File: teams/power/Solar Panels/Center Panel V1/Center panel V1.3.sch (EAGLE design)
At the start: 9 parts

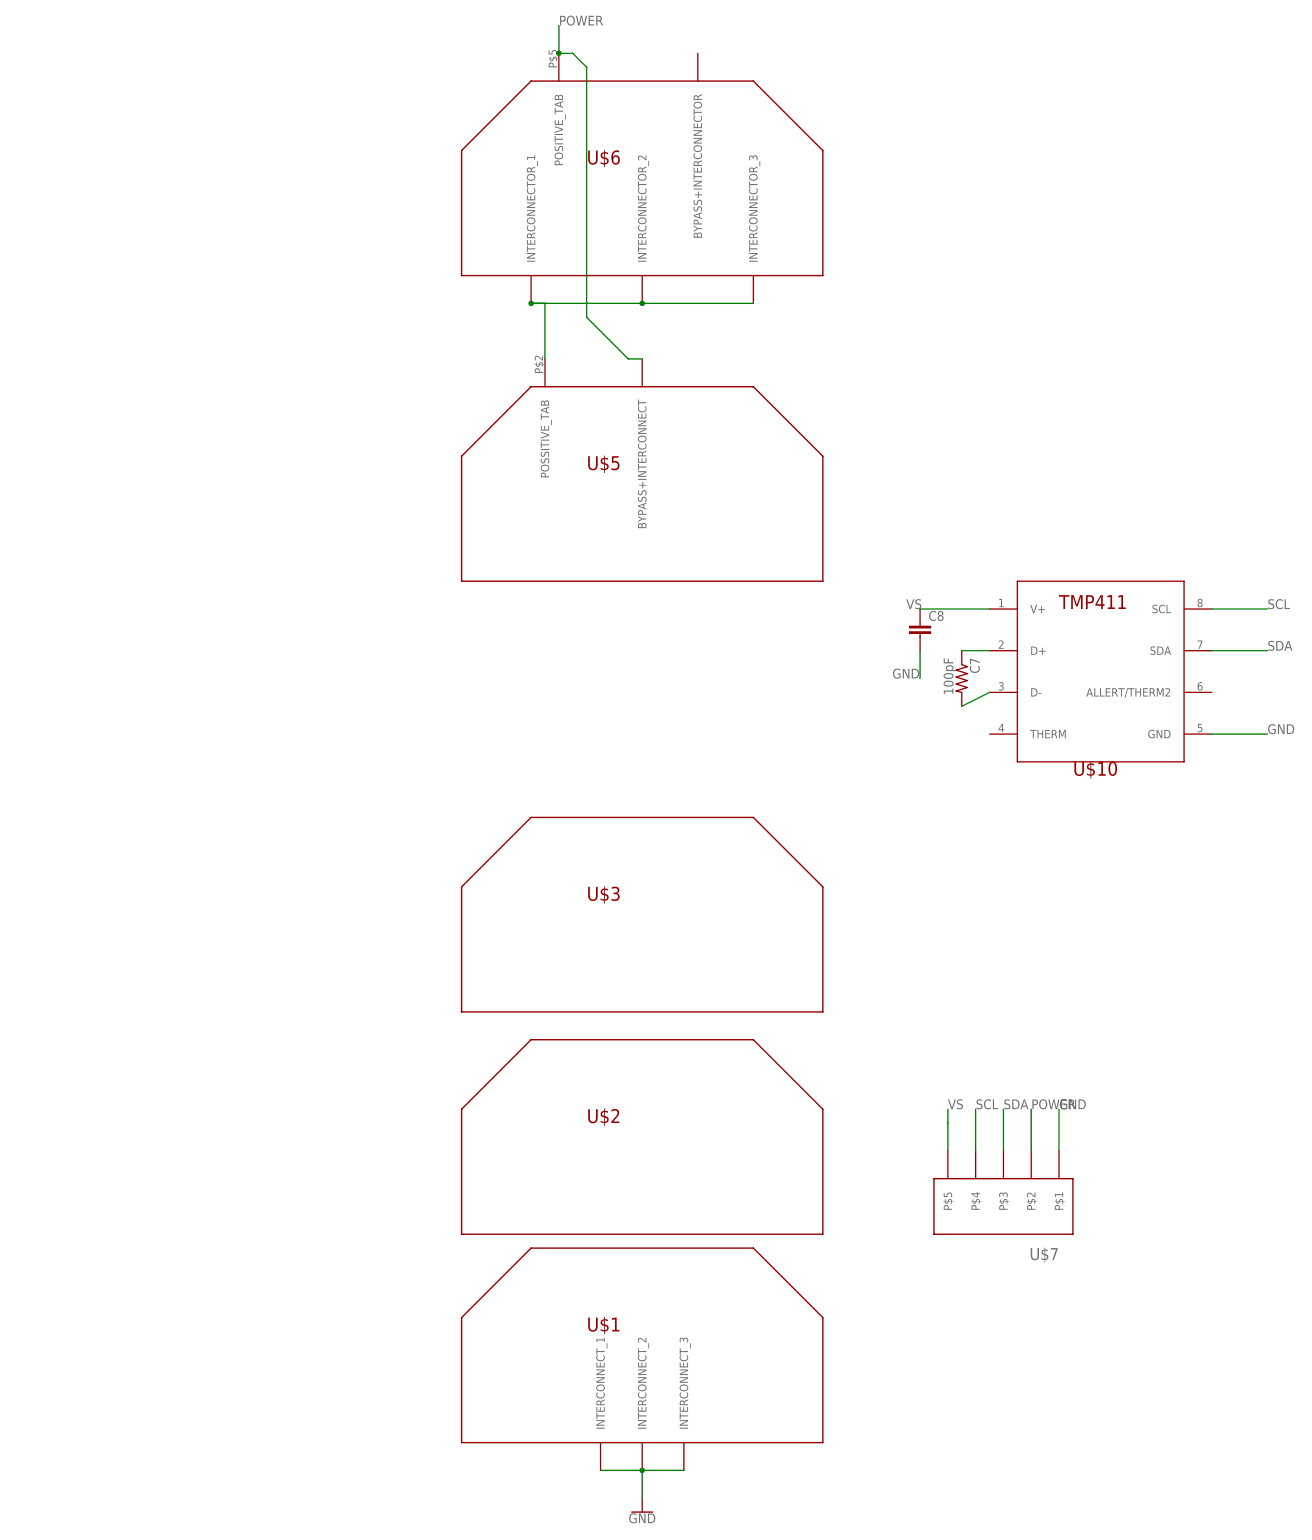
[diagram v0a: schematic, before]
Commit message: EPS/ old panels: Remove ground plane and changed temp sensor to TMP36
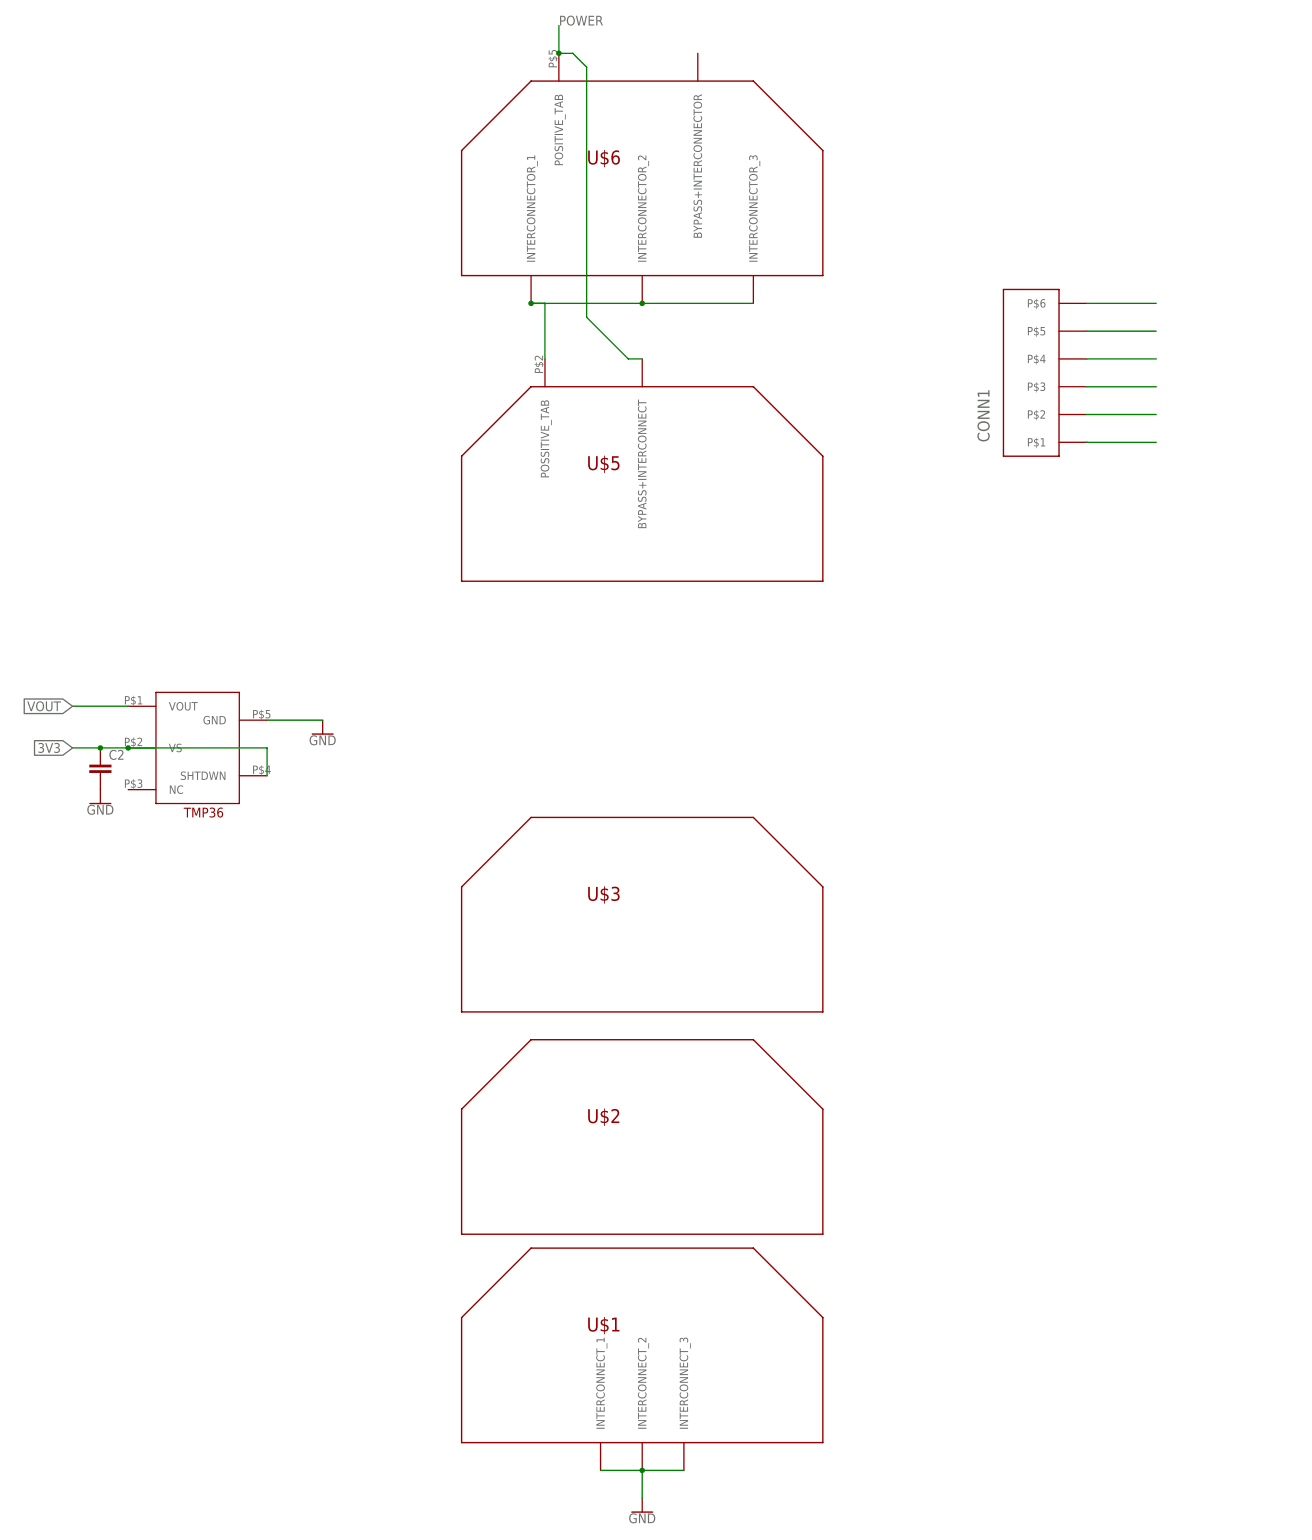
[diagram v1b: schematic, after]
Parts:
- removed C7: 100pF, Battery board V4.1 - simple signals:R-US_R0805
- removed C8: (no value), Battery board V4.1 - simple signals:C
- removed U$10: TMP411, DubSat1 Components:TMP411
- added C2: (no value), DubSat1 Components:CAPACITOR0805
- added CONN1: PICOLOCK_6, DubSat1 Components:PICOLOCK_6
- U$7: value PICOLOCK_5 -> TMP36; device DubSat1 Components:PICOLOCK_5 -> DubSat1 Components:TMP36
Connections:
- removed net N$14: C7.1, U$10.D+
- removed net N$15: C7.2, U$10.D-
- removed net SCL: U$10.SCL, U$7.P$4
- removed net SDA: U$10.SDA, U$7.P$3
- removed net VS: C8.1, U$10.V+, U$7.P$5
- new net 3V3: C2.1, CONN1.P$3, U$7.SHTDWN, U$7.VS
- new net VOUT: CONN1.P$4, U$7.VOUT
- net GND: now also CONN1.P$2, CONN1.P$5, U$7.GND; no longer C8.2, U$10.GND, U$7.P$1
- net POWER: now also CONN1.P$1, CONN1.P$6; no longer U$7.P$2
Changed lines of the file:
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@@
 <?xml version="1.0" encoding="utf-8"?>
 <!DOCTYPE eagle SYSTEM "eagle.dtd">
-<eagle version="8.3.1">
+<eagle version="8.5.0">
 <drawing>
 <settings>
@@
 <layer number="59" name="tCarbon" color="7" fill="1" visible="no" active="no"/>
 <layer number="60" name="bCarbon" color="7" fill="1" visible="no" active="no"/>
+<layer number="88" name="SimResults" color="9" fill="1" visible="yes" active="yes"/>
+<layer number="89" name="SimProbes" color="9" fill="1" visible="yes" active="yes"/>
 <layer number="90" name="Modules" color="5" fill="1" visible="yes" active="yes"/>
 <layer number="91" name="Nets" color="2" fill="1" visible="yes" active="yes"/>
@@
 <part name="U$6" library="DubSat1 Components" library_urn="urn:adsk.eagle:library:348159" deviceset="SOLAR_CELL_STAND-ALONE" device="" package3d_urn="urn:adsk.eagle:package:348283/2"/>
 <part name="GND1" library="SparkFun-PowerSymbols" deviceset="GND" device=""/>
-<part name="U$7" library="DubSat1 Components" library_urn="urn:adsk.eagle:library:348159" deviceset="PICOLOCK_5" device="" package3d_urn="urn:adsk.eagle:package:348289/2"/>
-<part name="U$10" library="DubSat1 Components" deviceset="TMP411" device=""/>
-<part name="C7" library="Battery board V4.1 - simple signals" deviceset="R-US_" device="R0805" value="100pF"/>
-<part name="C8" library="Battery board V4.1 - simple signals" deviceset="C" device=""/>
+<part name="U$7" library="DubSat1 Components" deviceset="TMP36" device=""/>
+<part name="C2" library="DubSat1 Components" deviceset="CAPACITOR" device="0805"/>
+<part name="GND4" library="SparkFun-PowerSymbols" deviceset="GND" device=""/>
+<part name="GND5" library="SparkFun-PowerSymbols" deviceset="GND" device=""/>
+<part name="CONN1" library="DubSat1 Components" deviceset="PICOLOCK_6" device=""/>
 </parts>
 <sheets>
@@
 <instance part="U$6" gate="G$1" x="0" y="213.36"/>
 <instance part="GND1" gate="1" x="33.02" y="-12.7"/>
-<instance part="U$7" gate="G$1" x="96.52" y="48.26" rot="R180"/>
-<instance part="U$10" gate="G$1" x="116.84" y="139.7"/>
-<instance part="C7" gate="G$1" x="91.44" y="139.7" rot="R270"/>
-<instance part="C8" gate="G$1" x="83.82" y="149.86"/>
+<instance part="U$7" gate="G$1" x="-48.26" y="127"/>
+<instance part="C2" gate="G$1" x="-66.04" y="121.92"/>
+<instance part="GND4" gate="1" x="-66.04" y="116.84"/>
+<instance part="GND5" gate="1" x="-25.4" y="129.54"/>
+<instance part="CONN1" gate="G$1" x="109.22" y="195.58" rot="R90"/>
 </instances>
 <busses>
@@
 </segment>
 <segment>
-<pinref part="U$7" gate="G$1" pin="P$1"/>
-<wire x1="109.22" y1="53.34" x2="109.22" y2="60.96" width="0.1524" layer="91"/>
-<label x="109.22" y="60.96" size="1.778" layer="95"/>
-</segment>
-<segment>
-<pinref part="U$10" gate="G$1" pin="GND"/>
-<wire x1="137.16" y1="129.54" x2="147.32" y2="129.54" width="0.1524" layer="91"/>
-<label x="147.32" y="129.54" size="1.778" layer="95"/>
-</segment>
-<segment>
-<pinref part="C8" gate="G$1" pin="2"/>
-<wire x1="83.82" y1="144.78" x2="83.82" y2="139.7" width="0.1524" layer="91"/>
-<label x="78.74" y="139.7" size="1.778" layer="95"/>
+<pinref part="U$7" gate="G$1" pin="GND"/>
+<wire x1="-35.56" y1="132.08" x2="-25.4" y2="132.08" width="0.1524" layer="91"/>
+<pinref part="GND5" gate="1" pin="GND"/>
+</segment>
+<segment>
+<pinref part="CONN1" gate="G$1" pin="P$5"/>
+<wire x1="114.3" y1="203.2" x2="127" y2="203.2" width="0.1524" layer="91"/>
+</segment>
+<segment>
+<pinref part="CONN1" gate="G$1" pin="P$2"/>
+<wire x1="114.3" y1="187.96" x2="127" y2="187.96" width="0.1524" layer="91"/>
 </segment>
 </net>
@@
 </segment>
 </net>
-<net name="VS" class="0">
-<segment>
-<pinref part="U$7" gate="G$1" pin="P$5"/>
-<wire x1="88.9" y1="53.34" x2="88.9" y2="58.42" width="0.1524" layer="91"/>
-<wire x1="88.9" y1="60.96" x2="88.9" y2="58.42" width="0.1524" layer="91"/>
-<label x="88.9" y="60.96" size="1.778" layer="95"/>
-</segment>
-<segment>
-<pinref part="U$10" gate="G$1" pin="V+"/>
-<wire x1="96.52" y1="152.4" x2="83.82" y2="152.4" width="0.1524" layer="91"/>
-<label x="81.28" y="152.4" size="1.778" layer="95"/>
-<pinref part="C8" gate="G$1" pin="1"/>
-</segment>
-</net>
-<net name="SDA" class="0">
-<segment>
-<pinref part="U$7" gate="G$1" pin="P$3"/>
-<wire x1="99.06" y1="53.34" x2="99.06" y2="60.96" width="0.1524" layer="91"/>
-<label x="99.06" y="60.96" size="1.778" layer="95"/>
-</segment>
-<segment>
-<pinref part="U$10" gate="G$1" pin="SDA"/>
-<wire x1="137.16" y1="144.78" x2="147.32" y2="144.78" width="0.1524" layer="91"/>
-<label x="147.32" y="144.78" size="1.778" layer="95"/>
-</segment>
-</net>
-<net name="SCL" class="0">
-<segment>
-<pinref part="U$7" gate="G$1" pin="P$4"/>
-<wire x1="93.98" y1="53.34" x2="93.98" y2="60.96" width="0.1524" layer="91"/>
-<label x="93.98" y="60.96" size="1.778" layer="95"/>
-</segment>
-<segment>
-<pinref part="U$10" gate="G$1" pin="SCL"/>
-<wire x1="137.16" y1="152.4" x2="147.32" y2="152.4" width="0.1524" layer="91"/>
-<label x="147.32" y="152.4" size="1.778" layer="95"/>
-</segment>
-</net>
 <net name="POWER" class="0">
-<segment>
-<pinref part="U$7" gate="G$1" pin="P$2"/>
-<wire x1="104.14" y1="53.34" x2="104.14" y2="60.96" width="0.1524" layer="91"/>
-<label x="104.14" y="60.96" size="1.778" layer="95"/>
-</segment>
 <segment>
 <pinref part="U$5" gate="G$1" pin="BYPASS+INTERCONNECT"/>
@@
 <label x="17.78" y="259.08" size="1.778" layer="95"/>
 </segment>
-</net>
-<net name="N$14" class="0">
-<segment>
-<pinref part="C7" gate="G$1" pin="1"/>
-<wire x1="91.44" y1="144.78" x2="96.52" y2="144.78" width="0.1524" layer="91"/>
-<pinref part="U$10" gate="G$1" pin="D+"/>
-</segment>
-</net>
-<net name="N$15" class="0">
-<segment>
-<pinref part="C7" gate="G$1" pin="2"/>
-<pinref part="U$10" gate="G$1" pin="D-"/>
-<wire x1="91.44" y1="134.62" x2="96.52" y2="137.16" width="0.1524" layer="91"/>
-</segment>
-</net>
+<segment>
+<pinref part="CONN1" gate="G$1" pin="P$6"/>
+<wire x1="114.3" y1="208.28" x2="127" y2="208.28" width="0.1524" layer="91"/>
+</segment>
+<segment>
+<pinref part="CONN1" gate="G$1" pin="P$1"/>
+<wire x1="114.3" y1="182.88" x2="127" y2="182.88" width="0.1524" layer="91"/>
+</segment>
+</net>
+<net name="VOUT" class="0">
+<segment>
+<pinref part="U$7" gate="G$1" pin="VOUT"/>
+<wire x1="-60.96" y1="134.62" x2="-71.12" y2="134.62" width="0.1524" layer="91"/>
+<label x="-71.12" y="134.62" size="1.778" layer="95" rot="R180" xref="yes"/>
+</segment>
+<segment>
+<pinref part="CONN1" gate="G$1" pin="P$4"/>
+<wire x1="114.3" y1="198.12" x2="127" y2="198.12" width="0.1524" layer="91"/>
+</segment>
+</net>
+<net name="3V3" class="0">
+<segment>
+<pinref part="U$7" gate="G$1" pin="VS"/>
+<wire x1="-60.96" y1="127" x2="-66.04" y2="127" width="0.1524" layer="91"/>
+<pinref part="C2" gate="G$1" pin="1"/>
+<wire x1="-66.04" y1="127" x2="-71.12" y2="127" width="0.1524" layer="91"/>
+<junction x="-66.04" y="127"/>
+<label x="-71.12" y="127" size="1.778" layer="95" rot="R180" xref="yes"/>
+<pinref part="U$7" gate="G$1" pin="SHTDWN"/>
+<wire x1="-60.96" y1="127" x2="-35.56" y2="127" width="0.1524" layer="91"/>
+<wire x1="-35.56" y1="127" x2="-35.56" y2="121.92" width="0.1524" layer="91"/>
+<junction x="-60.96" y="127"/>
+</segment>
+<segment>
+<pinref part="CONN1" gate="G$1" pin="P$3"/>
+<wire x1="114.3" y1="193.04" x2="127" y2="193.04" width="0.1524" layer="91"/>
+</segment>
+</net>
